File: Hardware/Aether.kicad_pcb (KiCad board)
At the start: 2 copper layers, 78 parts, among them J1 PRGM, J2 CONN-2, J3 CONN-2, J4 CONN-2, J5 CONN-2, J6 CONN-3, J7 CONN-3, Q1 IRLML6401, U1 ANTENOVA-UB, U2 ADF7012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

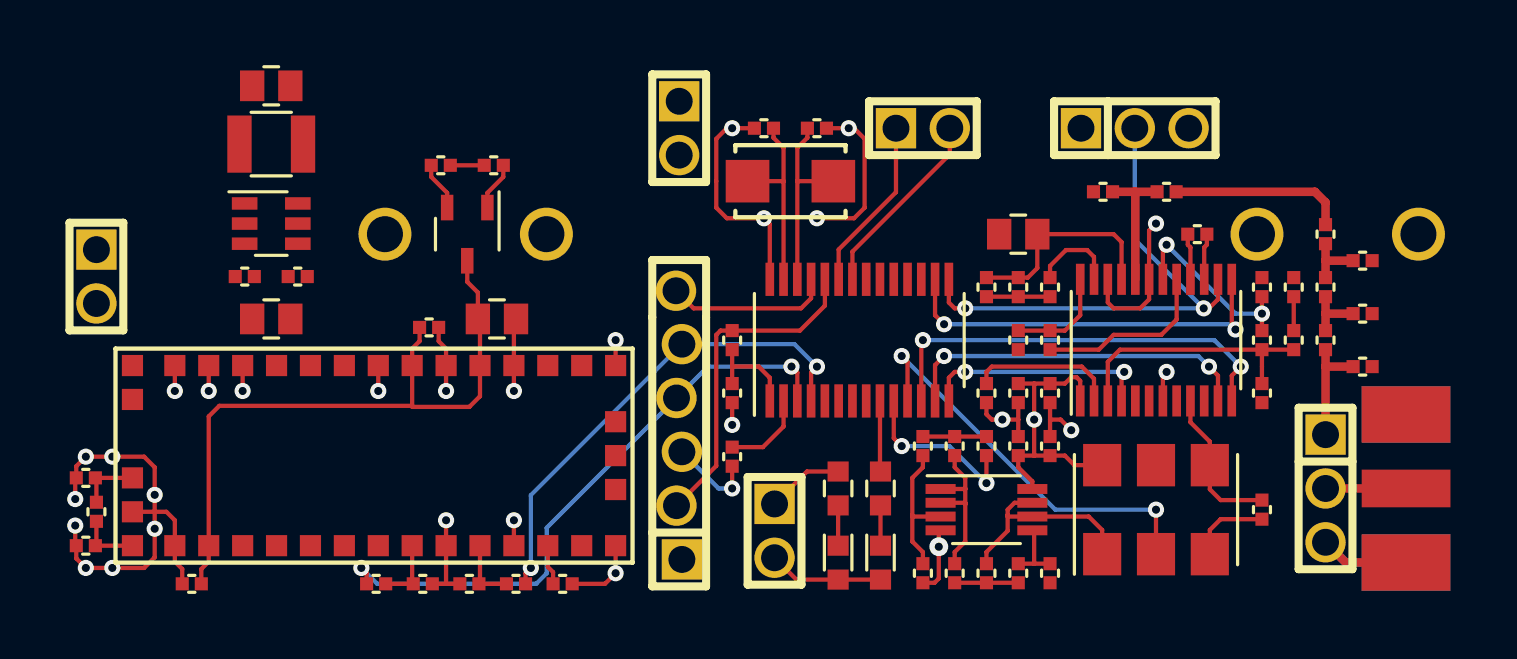
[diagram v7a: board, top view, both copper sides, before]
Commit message: Ground pour and rearrange expansion
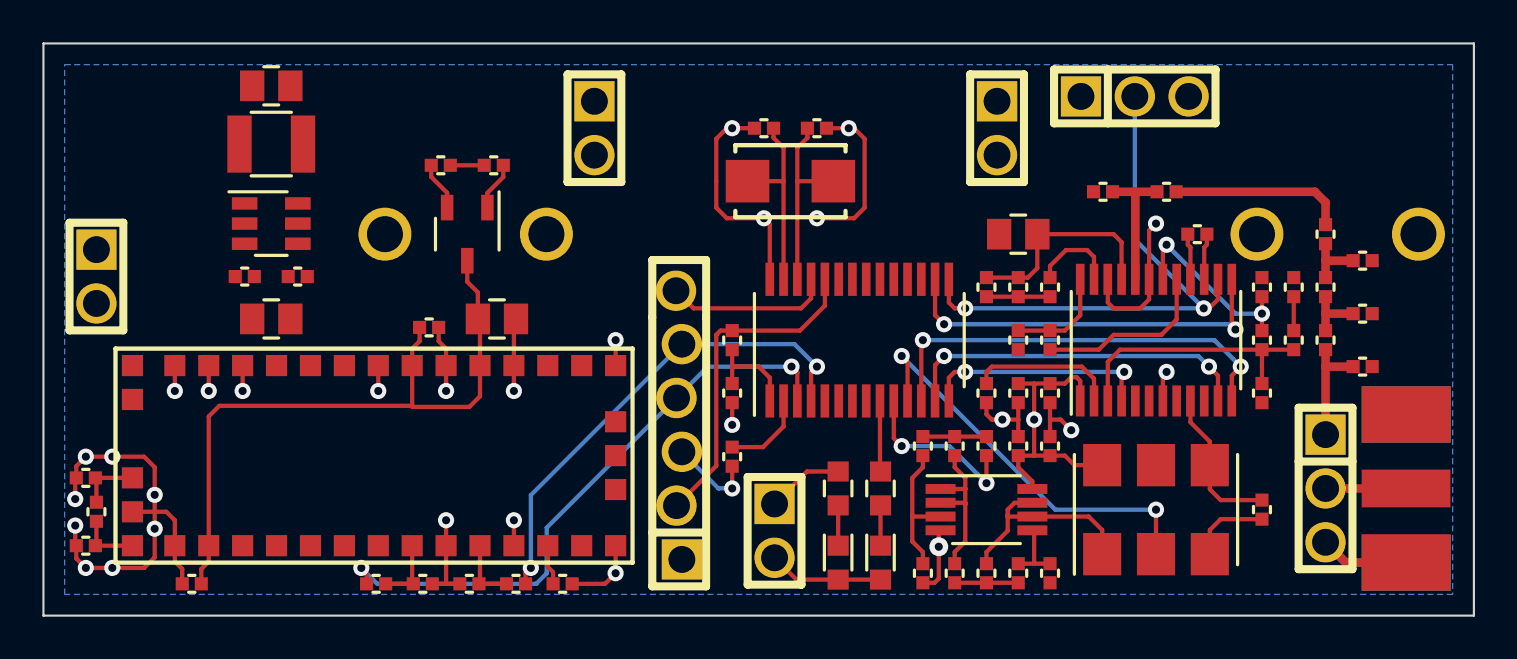
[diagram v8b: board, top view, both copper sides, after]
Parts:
- moved J3 4.00 mm to (154.0, 98.5)
- moved J5 3.50 mm to (173.0, 98.5), turned to 270 degrees
- moved J6 1.50 mm to (179.5, 97.0)
- turned R9 to 0 degrees
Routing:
- net /Core/SCL: track 9.03 -> 0.00 mm
- net /Core/SDA: track 8.25 -> 0.00 mm
- net /Core/TX_En: track 24.9 -> 26.4 mm
- added copper zone on B.Cu, net GND
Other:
- board outline added: 67.5 x 27 mm
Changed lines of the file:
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@@
   (general
     (links 180)
-    (no_connects 63)
+    (no_connects 39)
     (area 126.8424 93.0644 207.293981 122.9356)
     (thickness 1.6)
-    (drawings 0)
-    (tracks 416)
+    (drawings 4)
+    (tracks 410)
     (zones 0)
     (modules 78)
@@
   )
   (module RESC1005-N (layer F.Cu)
-    (at 140 105.5 180)
-    (fp_text reference R9 (at 0 -1.5 180) (layer F.SilkS) hide
+    (at 140 105.5)
+    (fp_text reference R9 (at 0 -1.5) (layer F.SilkS) hide
       (effects (font (size 1.27 0.762) (thickness 0.1524)))
     )
-    (fp_text value 10k (at 0 1.5 180) (layer F.SilkS) hide
+    (fp_text value 10k (at 0 1.5) (layer F.SilkS) hide
       (effects (font (size 1.27 0.762) (thickness 0.1524)))
     )
@@
     (fp_line (start 0.95 0.5) (end 0.95 -0.5) (layer Eco1.User) (width 0.0762))
     (fp_line (start 0.95 -0.5) (end -0.95 -0.5) (layer Eco1.User) (width 0.0762))
-    (pad 1 smd rect (at -0.45 0 180) (size 0.62 0.62)
+    (pad 1 smd rect (at -0.45 0) (size 0.62 0.62)
       (layers F.Cu F.Paste F.Mask)
       (net 55 N-0000078)
     )
-    (pad 2 smd rect (at 0.45 0 180) (size 0.62 0.62)
+    (pad 2 smd rect (at 0.45 0) (size 0.62 0.62)
       (layers F.Cu F.Paste F.Mask)
       (net 3 +BATT)
@@
   )
   (module HDRV2W38P254_2X1 (layer F.Cu)
-    (at 169.5 98.5)
-    (fp_text reference J5 (at 0 -2.54) (layer F.SilkS) hide
+    (at 173 98.5 270)
+    (fp_text reference J5 (at 0 -2.54 270) (layer F.SilkS) hide
       (effects (font (size 1.524 1.524) (thickness 0.3048)))
     )
-    (fp_text value CONN-2 (at 0 2.54) (layer F.SilkS) hide
+    (fp_text value CONN-2 (at 0 2.54 270) (layer F.SilkS) hide
       (effects (font (size 1.524 1.524) (thickness 0.3048)))
     )
@@
     (fp_line (start 2.54 1.27) (end -2.54 1.27) (layer F.SilkS) (width 0.381))
     (fp_line (start -2.54 1.27) (end -2.54 -1.27) (layer F.SilkS) (width 0.381))
-    (pad 1 thru_hole rect (at -1.27 0) (size 1.905 1.905) (drill 1.27)
+    (pad 1 thru_hole rect (at -1.27 0 270) (size 1.905 1.905) (drill 1.27)
       (layers *.Cu *.Mask F.SilkS)
       (net 14 /Core/SDA)
     )
-    (pad 2 thru_hole circle (at 1.27 0) (size 1.905 1.905) (drill 1.27)
+    (pad 2 thru_hole circle (at 1.27 0 270) (size 1.905 1.905) (drill 1.27)
       (layers *.Cu *.Mask F.SilkS)
       (net 13 /Core/SCL)
@@
   )
   (module HDRV2W38P254_2X1 (layer F.Cu)
-    (at 158 98.5 270)
+    (at 154 98.5 270)
     (fp_text reference J3 (at 0 -2.54 270) (layer F.SilkS) hide
       (effects (font (size 1.524 1.524) (thickness 0.3048)))
@@
   )
   (module HDRV3W38P254_3X1 (layer F.Cu)
-    (at 179.5 98.5)
+    (at 179.5 97)
     (fp_text reference J6 (at 0 -2.54) (layer F.SilkS) hide
       (effects (font (size 1.524 1.524) (thickness 0.3048)))
@@
     )
   )
+  (gr_line (start 195.5 94.5) (end 195.5 121.5) (angle 90) (layer Edge.Cuts) (width 0.1))
+  (gr_line (start 128 94.5) (end 195.5 94.5) (angle 90) (layer Edge.Cuts) (width 0.1))
+  (gr_line (start 128 121.5) (end 128 94.5) (angle 90) (layer Edge.Cuts) (width 0.1))
+  (gr_line (start 195.5 121.5) (end 128 121.5) (angle 90) (layer Edge.Cuts) (width 0.1))
   (segment (start 146.3 100.25) (end 146.3 100.8) (width 0.2032) (layer F.Cu) (net 1))
   (segment (start 147.05 101.55) (end 147.05 102.245) (width 0.2032) (layer F.Cu) (net 1))
@@
   (via (at 170.5 109.25) (size 0.762) (layers F.Cu B.Cu) (net 12))
   (segment (start 170.075 109.675) (end 170.5 109.25) (width 0.2032) (layer F.Cu) (net 12))
-  (segment (start 166.175 105.63) (end 166.175 104.325) (width 0.2032) (layer F.Cu) (net 13))
-  (segment (start 170.77 99.73) (end 170.77 98.5) (width 0.2032) (layer F.Cu) (net 13))
-  (segment (start 166.175 104.325) (end 170.77 99.73) (width 0.2032) (layer F.Cu) (net 13))
-  (segment (start 165.525 105.63) (end 165.525 104.225) (width 0.2032) (layer F.Cu) (net 14))
-  (segment (start 168.23 101.52) (end 168.23 98.5) (width 0.2032) (layer F.Cu) (net 14))
-  (segment (start 165.525 104.225) (end 168.23 101.52) (width 0.2032) (layer F.Cu) (net 14))
   (segment (start 184.075 105.63) (end 184.075 107.825) (width 0.2032) (layer F.Cu) (net 15))
   (segment (start 170.075 107.325) (end 170.075 105.63) (width 0.2032) (layer F.Cu) (net 15))
@@
   (via (at 171.5 110) (size 0.762) (layers F.Cu B.Cu) (net 19))
   (segment (start 171 110) (end 171.5 110) (width 0.2032) (layer F.Cu) (net 19))
-  (segment (start 182.75 107) (end 179.5 103.75) (width 0.2032) (layer B.Cu) (net 20))
-  (segment (start 179.5 103.75) (end 179.5 98.5) (width 0.2032) (layer B.Cu) (net 20))
+  (segment (start 179.5 97) (end 179.5 103.75) (width 0.2032) (layer B.Cu) (net 20))
+  (segment (start 179.5 103.75) (end 182.75 107) (width 0.2032) (layer B.Cu) (net 20))
   (segment (start 183.425 105.63) (end 183.425 106.575) (width 0.2032) (layer F.Cu) (net 20))
   (segment (start 170.725 106.725) (end 170.725 105.63) (width 0.2032) (layer F.Cu) (net 20))
@@
   (segment (start 171.5 115.5) (end 171.5 115) (width 0.2032) (layer F.Cu) (net 56))
   (segment (start 171 118.5) (end 171.5 118) (width 0.2032) (layer F.Cu) (net 56))
+  (zone (net 30) (net_name GND) (layer B.Cu) (hatch edge 0.508)
+    (connect_pads (clearance 0.2032))
+    (min_thickness 0.2032)
+    (fill (arc_segments 16) (thermal_gap 0.2032) (thermal_bridge_width 0.3048))
+    (polygon
+      (pts
+        (xy 194.5 120.5) (xy 129 120.5) (xy 129 95.5) (xy 194.5 95.5)
+      )
+    )
+  )
 )
